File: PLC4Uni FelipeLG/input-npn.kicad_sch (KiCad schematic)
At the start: 3 parts, among them Q1 BFN26

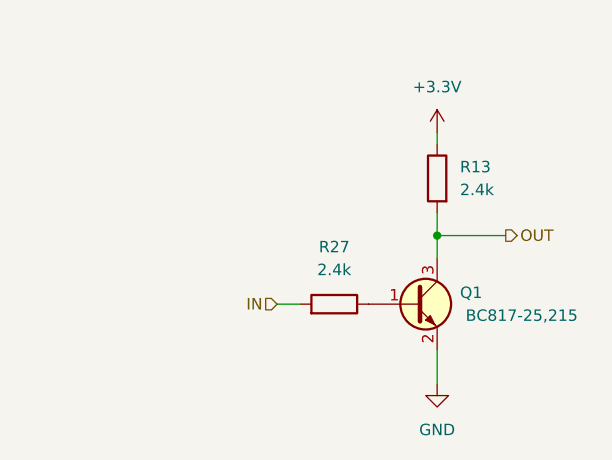
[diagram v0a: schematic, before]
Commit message: Add files via upload
Updated Circuitos corregidos y pistas agregadas
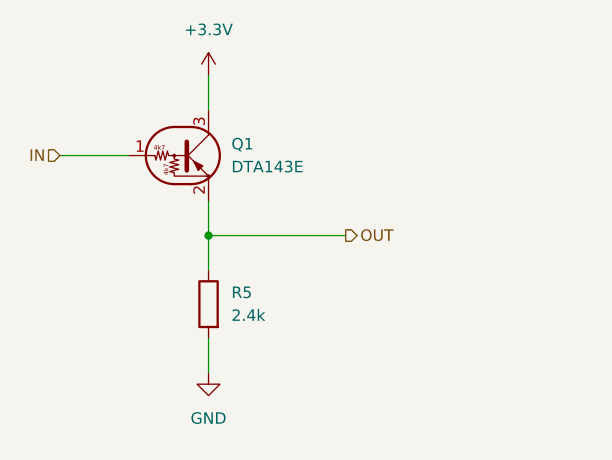
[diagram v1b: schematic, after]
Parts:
- removed Q1: BFN26, Package_TO_SOT_SMD_AKL:SOT-23, symbol Transistor_BJT_AKL:BFN26
- removed R13, R27: 2.4k, Resistor_SMD_AKL:R_0603_1608Metric, symbol Resistor_AKL:R_0603
- added Q1: DTA143E, Package_TO_SOT_SMD_AKL:SC-59, symbol Transistor_BJT:DTA143E
- added R5: 2.4k, Resistor_SMD_AKL:R_0603_1608Metric, symbol Resistor_AKL:R_0603
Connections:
- net +3.3V: now also Q1.3 (C)
- net GND: now also R5.1
- net IN: now also Q1.1 (B)
- net OUT: now also Q1.2 (E), R5.2
